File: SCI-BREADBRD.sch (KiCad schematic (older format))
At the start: 0 parts

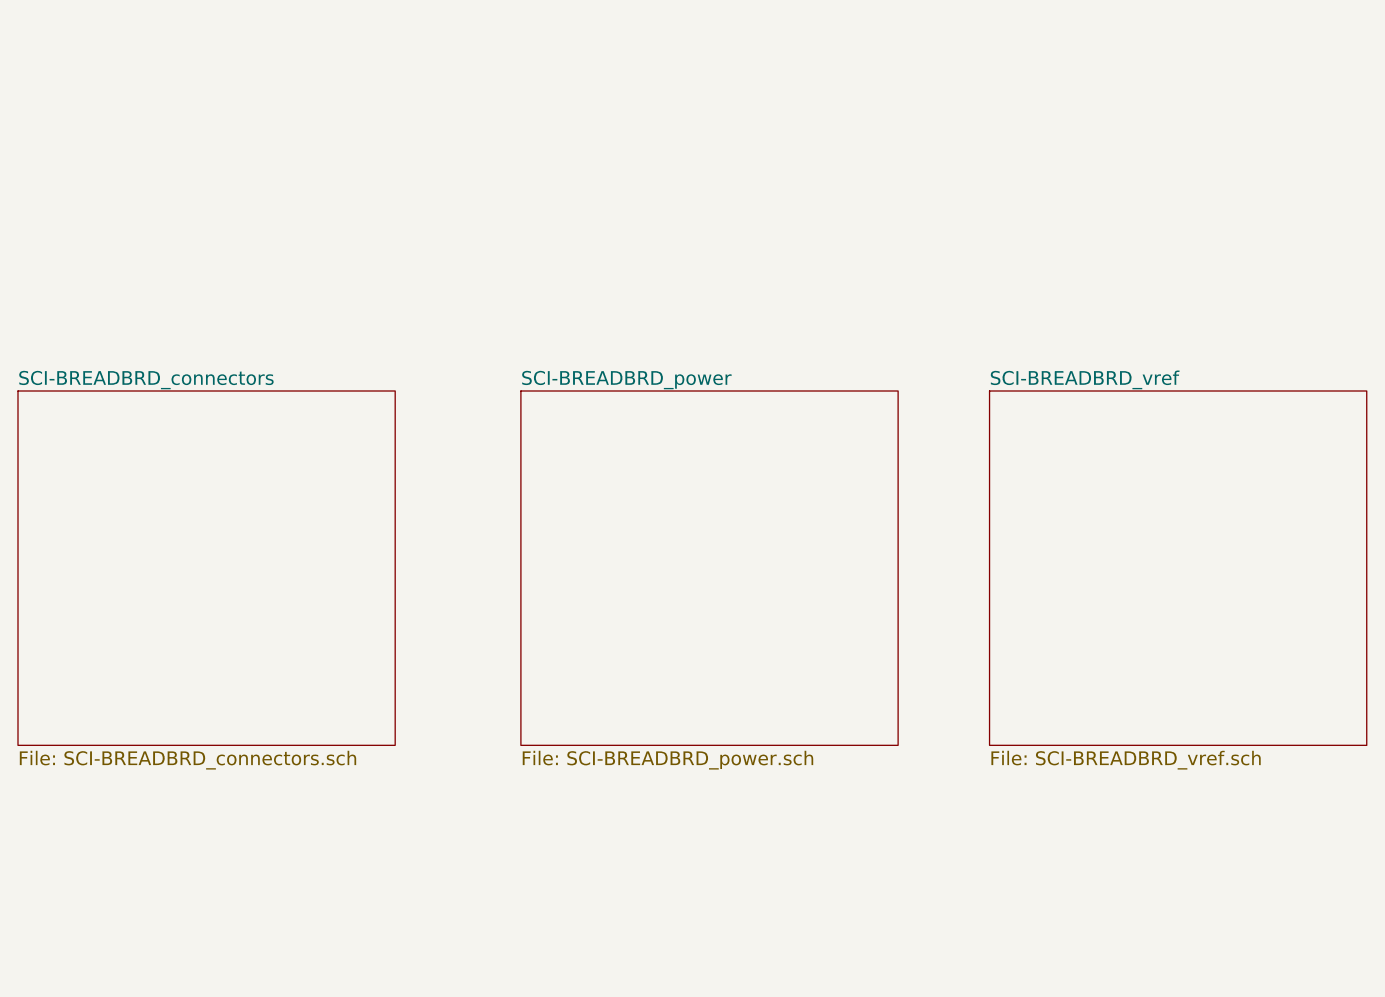
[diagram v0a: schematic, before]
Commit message: Completed ERC. Added some power flags and fixed mis-connected pins.
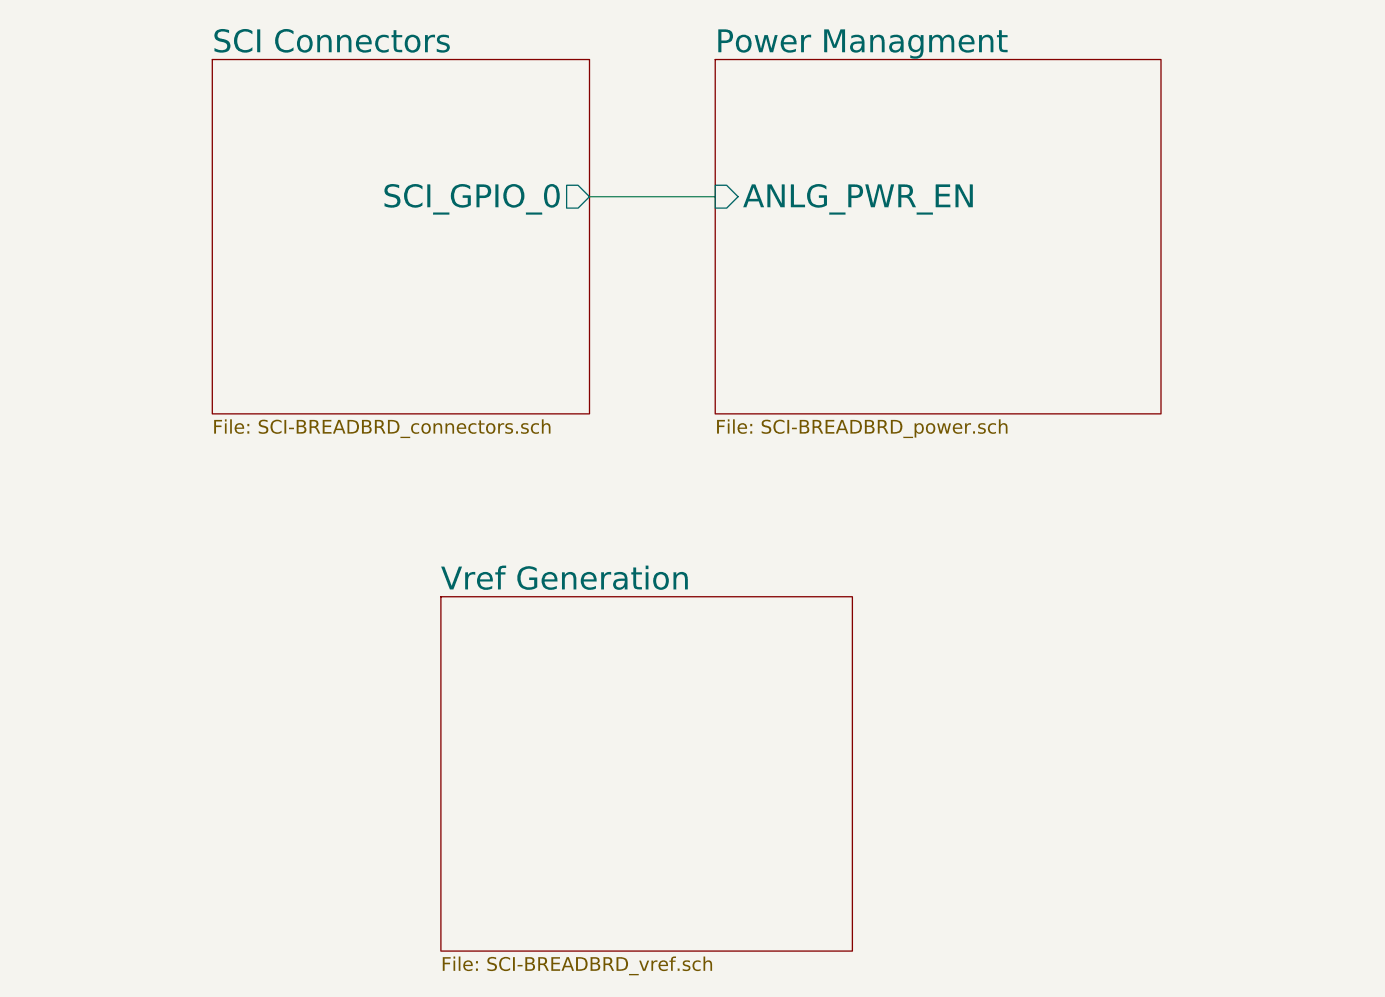
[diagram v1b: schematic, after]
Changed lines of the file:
@@
-EESchema Schematic File Version 2  date Fri 27 Apr 2012 09:11:54 AM EDT
+EESchema Schematic File Version 2  date Fri 27 Apr 2012 11:11:24 AM EDT
 LIBS:custom_transistors
 LIBS:TI_custom
@@
 $EndDescr
 $Sheet
-S 2650 3350 1650 1550
+S 3500 1900 1650 1550
 U 4F8C584B
-F0 "SCI-BREADBRD_connectors" 60
+F0 "SCI Connectors" 100
 F1 "SCI-BREADBRD_connectors.sch" 60
+F2 "SCI_GPIO_0" O R 5150 2500 100
 $EndSheet
 $Sheet
-S 4850 3350 1650 1550
+S 5700 1900 1950 1550
 U 4F8C5AD7
-F0 "SCI-BREADBRD_power" 60
+F0 "Power Managment" 100
 F1 "SCI-BREADBRD_power.sch" 60
+F2 "ANLG_PWR_EN" I L 5700 2500 100
 $EndSheet
 $Sheet
-S 6900 3350 1650 1550
+S 4500 4250 1800 1550
 U 4F8DDD4C
-F0 "SCI-BREADBRD_vref" 60
+F0 "Vref Generation" 100
 F1 "SCI-BREADBRD_vref.sch" 60
 $EndSheet
+Wire Wire Line
+	5150 2500 5700 2500
 $EndSCHEMATC
